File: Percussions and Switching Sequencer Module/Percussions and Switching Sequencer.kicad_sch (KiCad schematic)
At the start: 93 parts, among them U2 4051, U4 40106

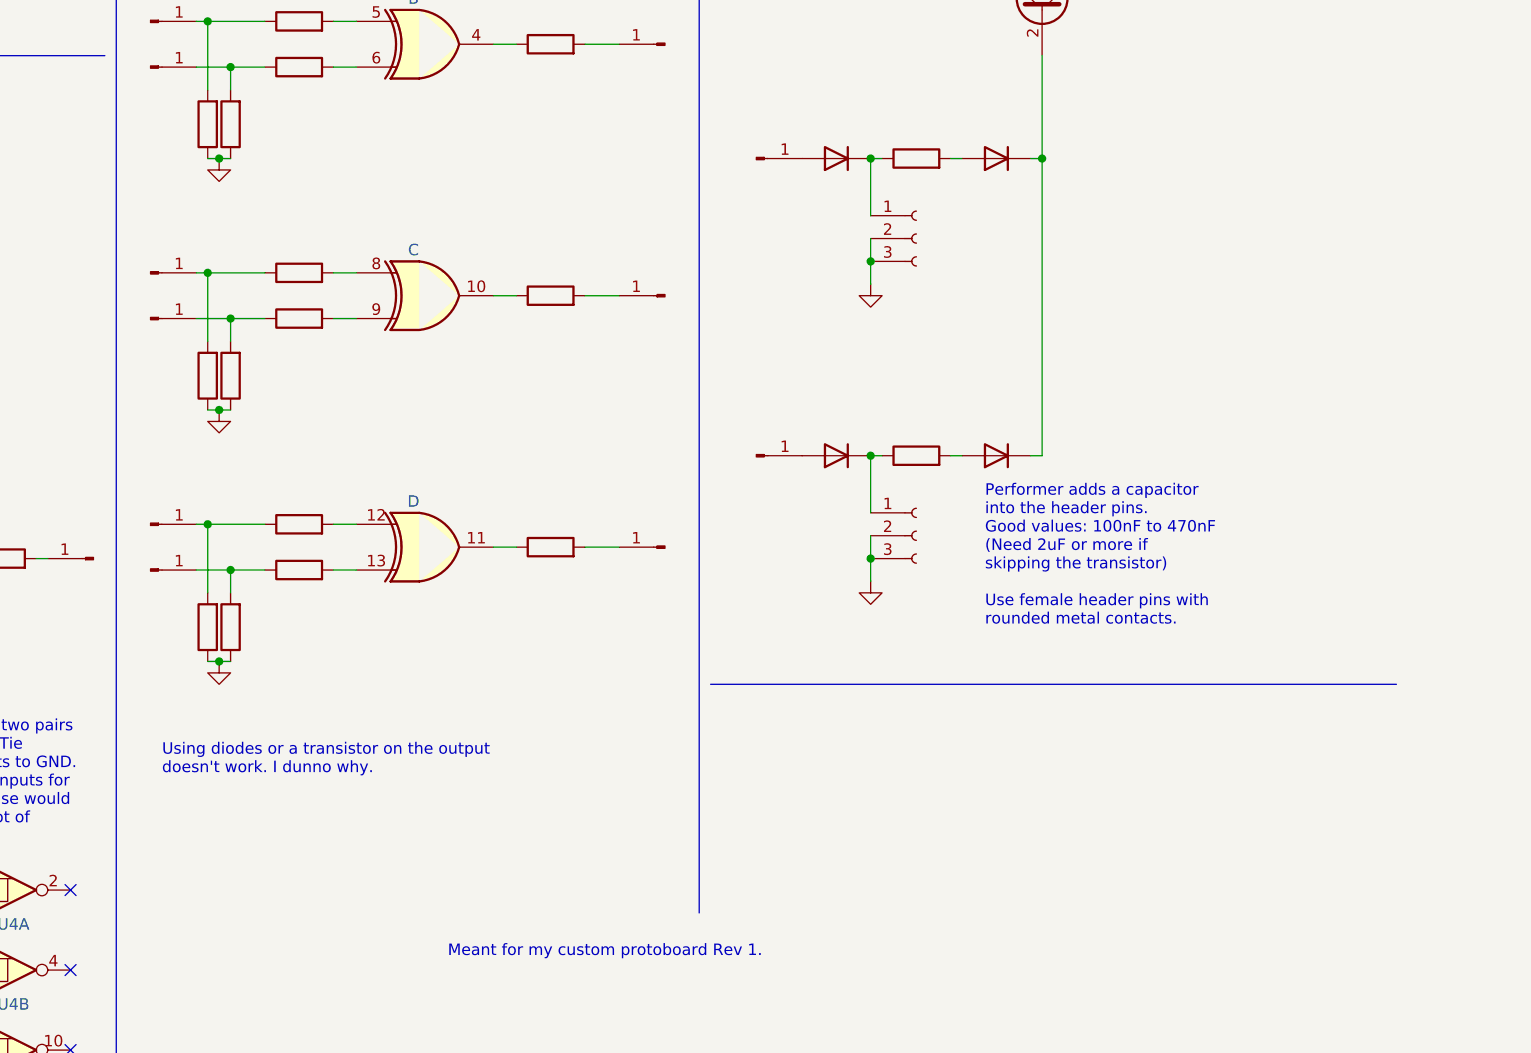
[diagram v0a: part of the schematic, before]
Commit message: Add switching sequencer to module
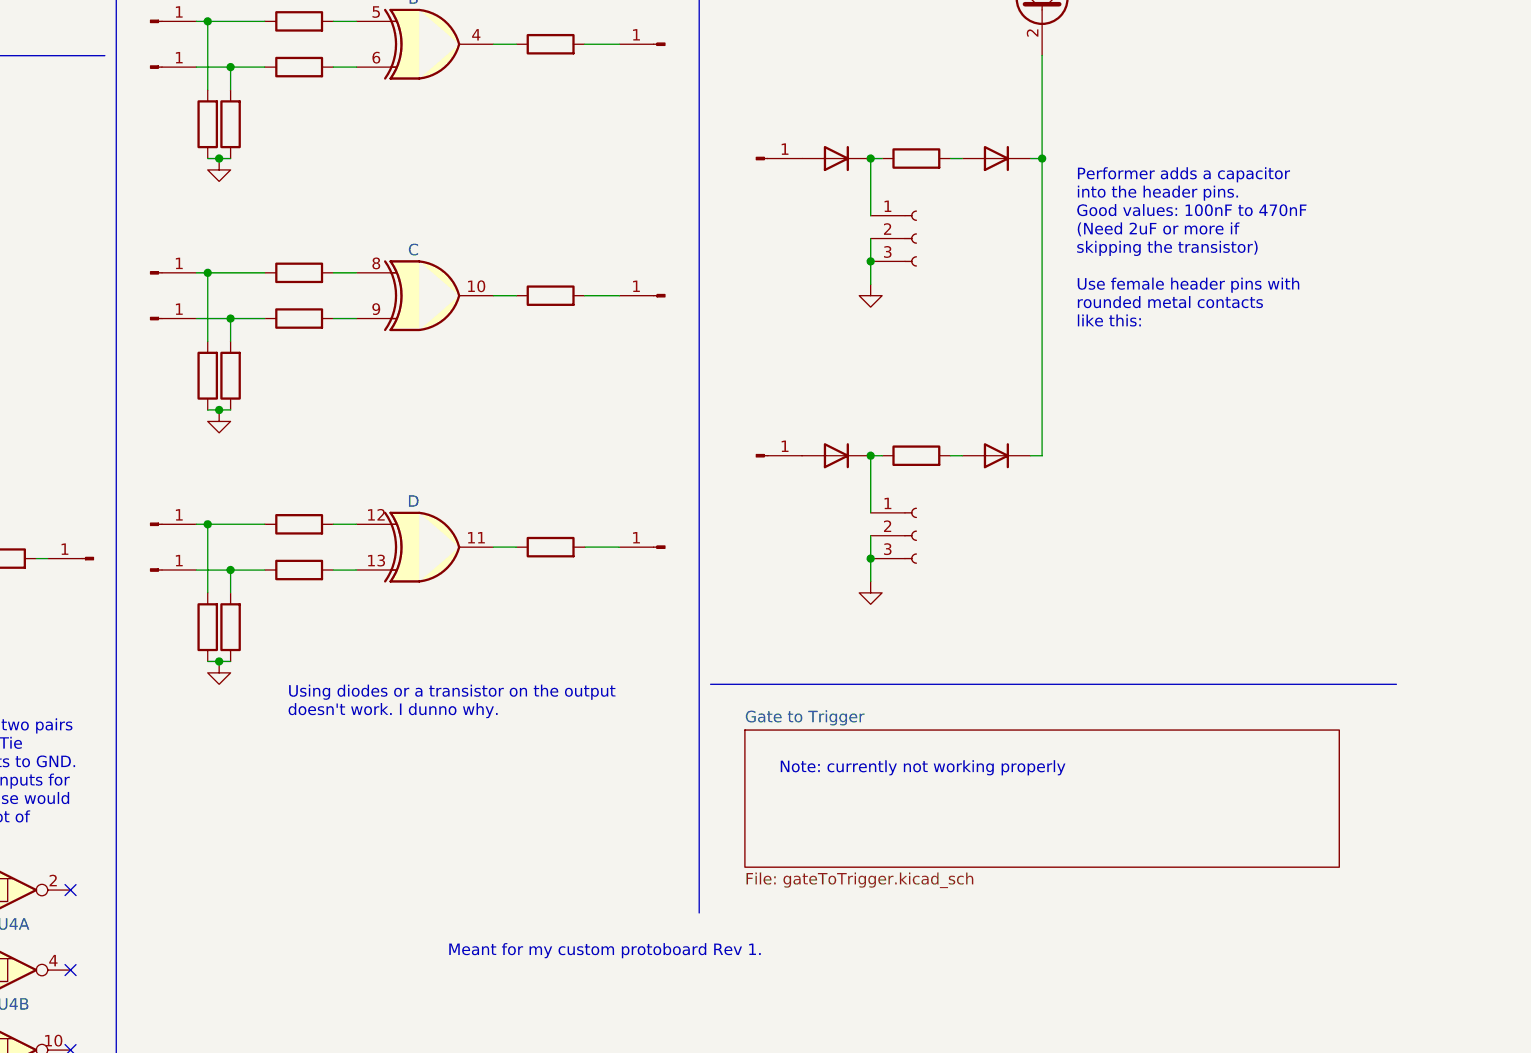
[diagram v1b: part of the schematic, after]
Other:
- added sheet Gate to Trigger (gateToTrigger.kicad_sch)
- note added: "Note: currently not working properly"
- note added: "Performer adds a capacitor into the header pins. Good values: 100nF to 470nF (Need 2uF or more if skipping the transistor) Use female header pins with rounded metal contacts like this:"
- note removed: "Performer adds a capacitor into the header pins. Good values: 100nF to 470nF (Need 2uF or more if skipping the transistor) Use female header pins with rounded metal contacts."
